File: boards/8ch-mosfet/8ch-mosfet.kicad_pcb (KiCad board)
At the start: 2 copper layers, 184.5 x 137 mm, 148 parts, among them J1 N2K, J10 Screw_Terminal_01x02, J11 Screw_Terminal_01x02, J12 Screw_Terminal_01x02, J2 I2C, J3 Screw_Terminal_01x08, J5 Screw_Terminal_01x02, J6 Screw_Terminal_01x02, J7 Screw_Terminal_01x02, J8 Screw_Terminal_01x02, J9 Screw_Terminal_01x02, M1 Fan_4pin, Q1 BC817, Q10 IRF4905, Q11 BC817, Q12 IRF4905, Q13 BC817, Q14 IRF4905, Q15 BC817, Q16 IRF4905, Q2 IRF4905, Q3 BC817, Q4 IRF4905, Q5 BC817, Q6 IRF4905, Q7 BC817, Q8 IRF4905, Q9 BC817, U1 ESP32-DEVKITC, U10 ACS725xLCTR-20AU, U11 ACS725xLCTR-20AU, U12 ACS725xLCTR-20AU, U2 MCP3208, U3 R-78B3.3-2.0, U5 ACS725xLCTR-20AU, U6 ACS725xLCTR-20AU, U7 ACS725xLCTR-20AU, U8 ACS725xLCTR-20AU, U9 ACS725xLCTR-20AU

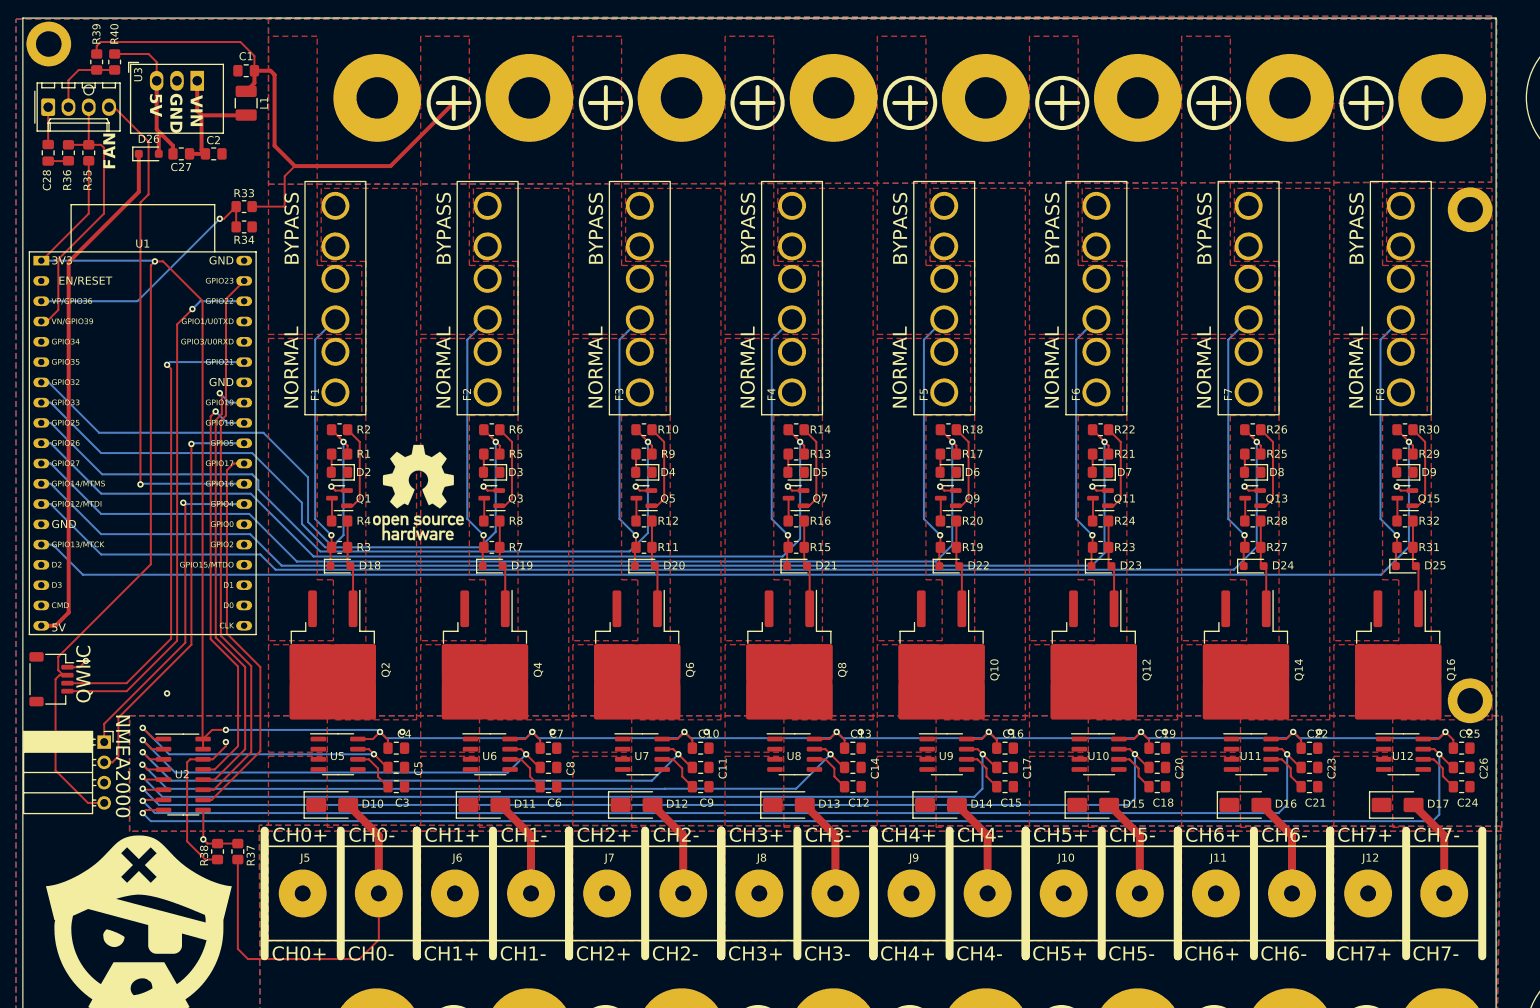
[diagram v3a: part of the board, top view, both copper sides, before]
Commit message: added 2nd fan header and simplified circuit.
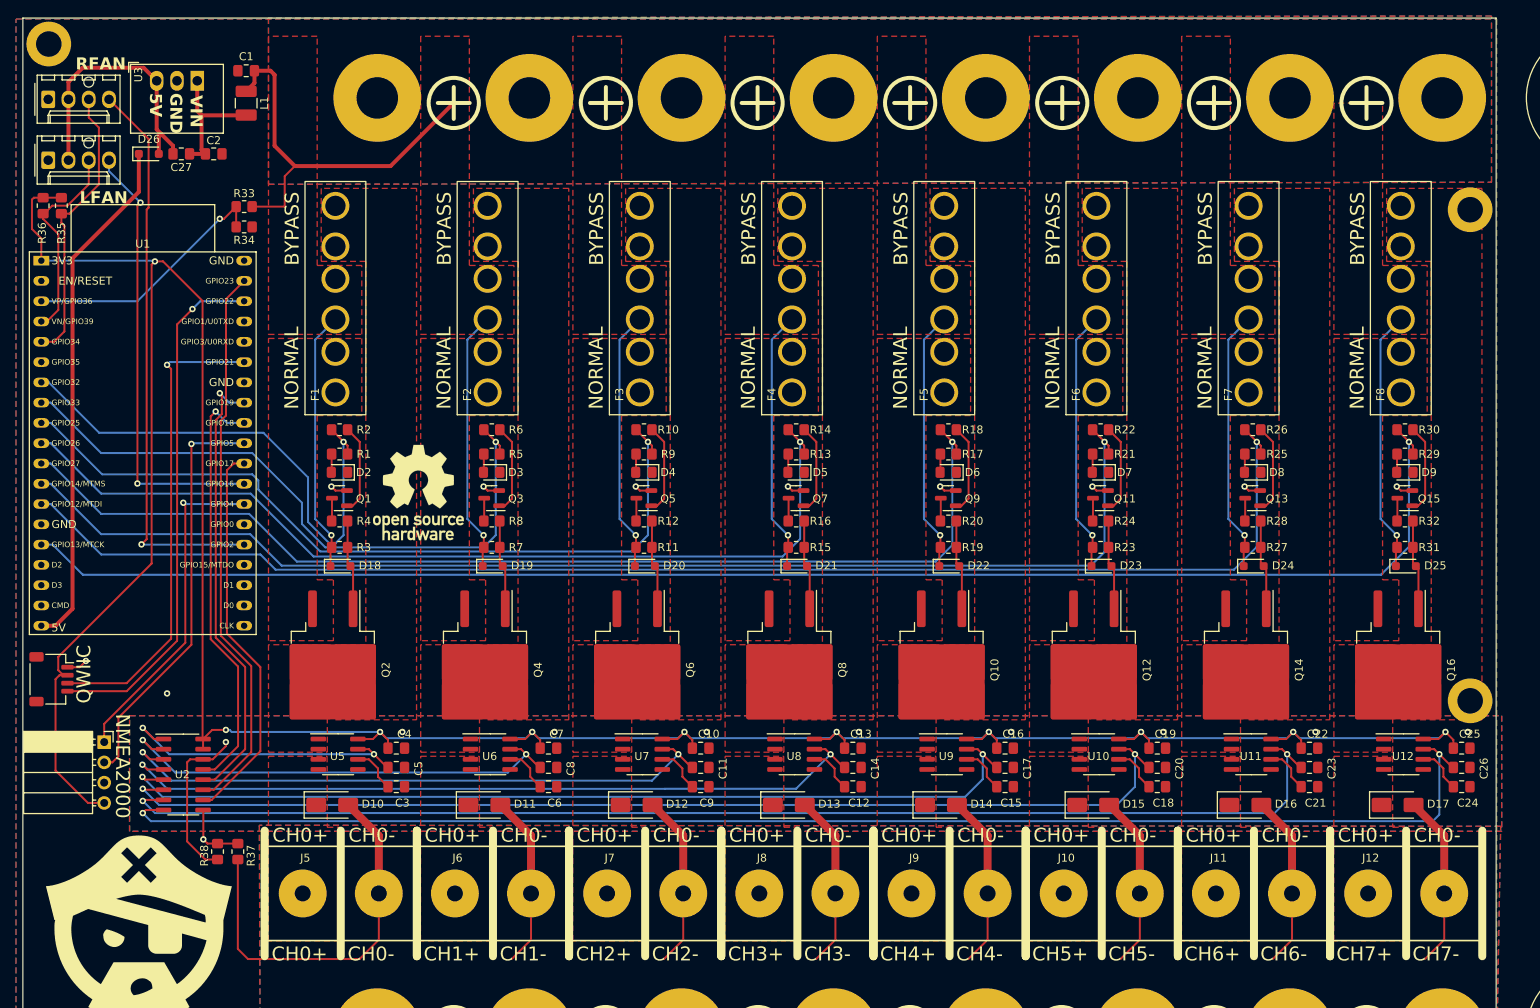
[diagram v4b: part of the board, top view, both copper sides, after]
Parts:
- removed C28: 1nF, Capacitor_SMD:C_0805_2012Metric_Pad1.18x1.45mm_HandSolder
- removed R39, R40: 0R, Resistor_SMD:R_0805_2012Metric_Pad1.20x1.40mm_HandSolder
- added M2: Fan_4pin, gnarboard:Molex 0470531000, F.Cu at (3.17, 17.8)
- R35: value 10k -> 1k
- R36: value 3.3k -> 1k
- moved R35 7.46 mm to (4.83, 23.5), turned to 90 degrees
- moved R36 7.34 mm to (2.54, 23.5)
- moved M1 0.98 mm to (3.17, 10.2)
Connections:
- M1 pad 2: Net-(M1-+) -> +5V
- M1 pad 3: FAN_TACHO -> FAN_TACH2
- M1 pad 4: FAN_PWM -> FAN_PWM2
- R35 pad 1: FAN_TACHO -> FAN_TACH2
- R36 pad 1: Net-(C28-Pad1) -> FAN_TACH1
- R36 pad 2: FAN_TACHO -> +3.3V
- U1 pad 24: unconnected-(U1-GPIO2-Pad24) -> FAN_PWM2
- U1 pad 27: FAN_PWM -> FAN_PWM1
- U1 pad 4: FAN_TACHO -> FAN_TACH1
- U1 pad 5: unconnected-(U1-GPIO34-Pad5) -> FAN_TACH2
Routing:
- net FAN_PWM2: track 0.00 -> 71.0 mm, vias 0 -> 1
- net GNDPWR: track 137.5 -> 202.1 mm
- net FAN_PWM: track 63.1 -> 0.00 mm, vias 1 -> 0
- net FAN_PWM1: track 0.00 -> 55.7 mm, vias 0 -> 2
- net FAN_TACH2: track 0.00 -> 35.7 mm
- net FAN_TACHO: track 34.7 -> 0.00 mm
- net FAN_TACH1: track 0.00 -> 25.8 mm
- net +24V: track 339.5 -> 316.0 mm
- net +5V: track 20.7 -> 34.9 mm
- net Net-(M1-+): track 9.69 -> 0.00 mm
- net GNDD: track 32.9 -> 28.3 mm
- net +3.3V: track 377.3 -> 374.3 mm
- net Net-(C28-Pad1): track 2.56 -> 0.00 mm
- net /ADC5: track 138.3 -> 137.5 mm
- net /ADC4: track 118.5 -> 117.8 mm
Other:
- board text added: "LFAN"
- board text added: "RFAN"
- board text removed: "FAN"

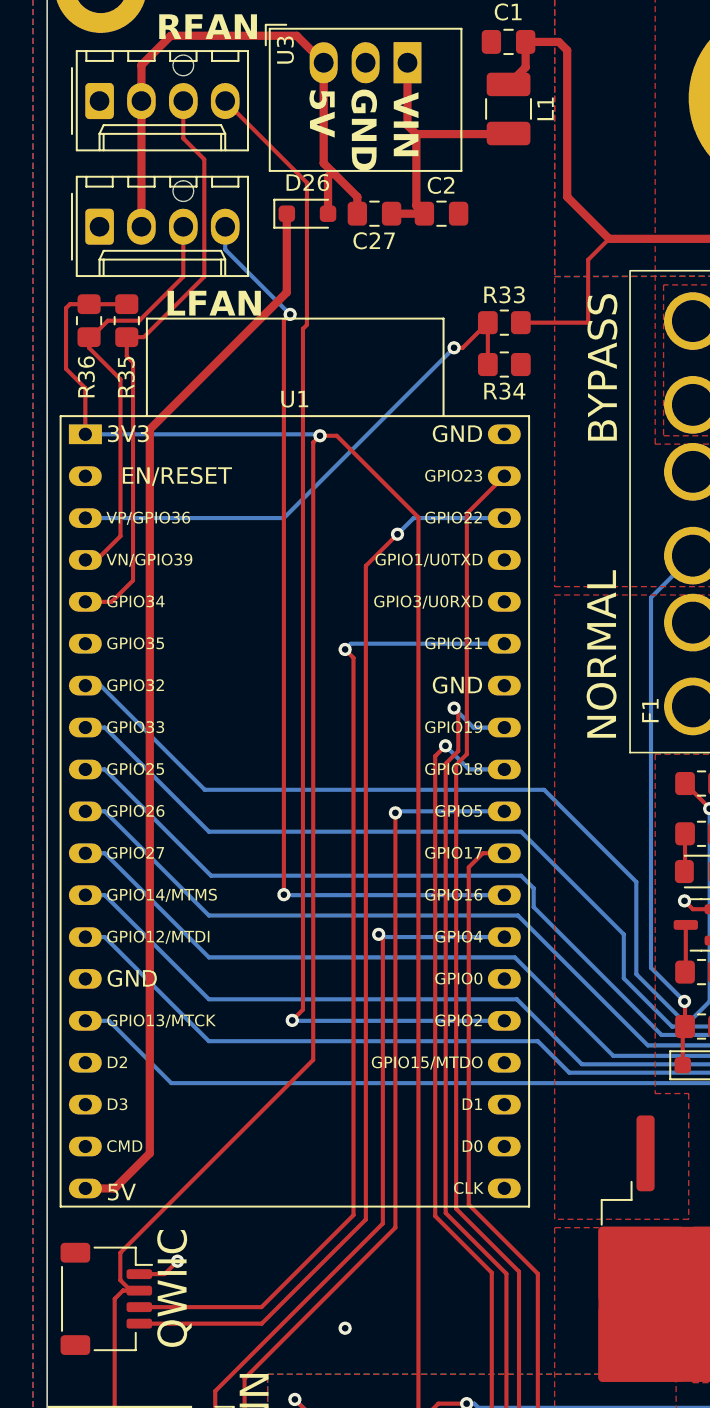
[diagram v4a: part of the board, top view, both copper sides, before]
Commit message: added a better adc for getting bus voltage
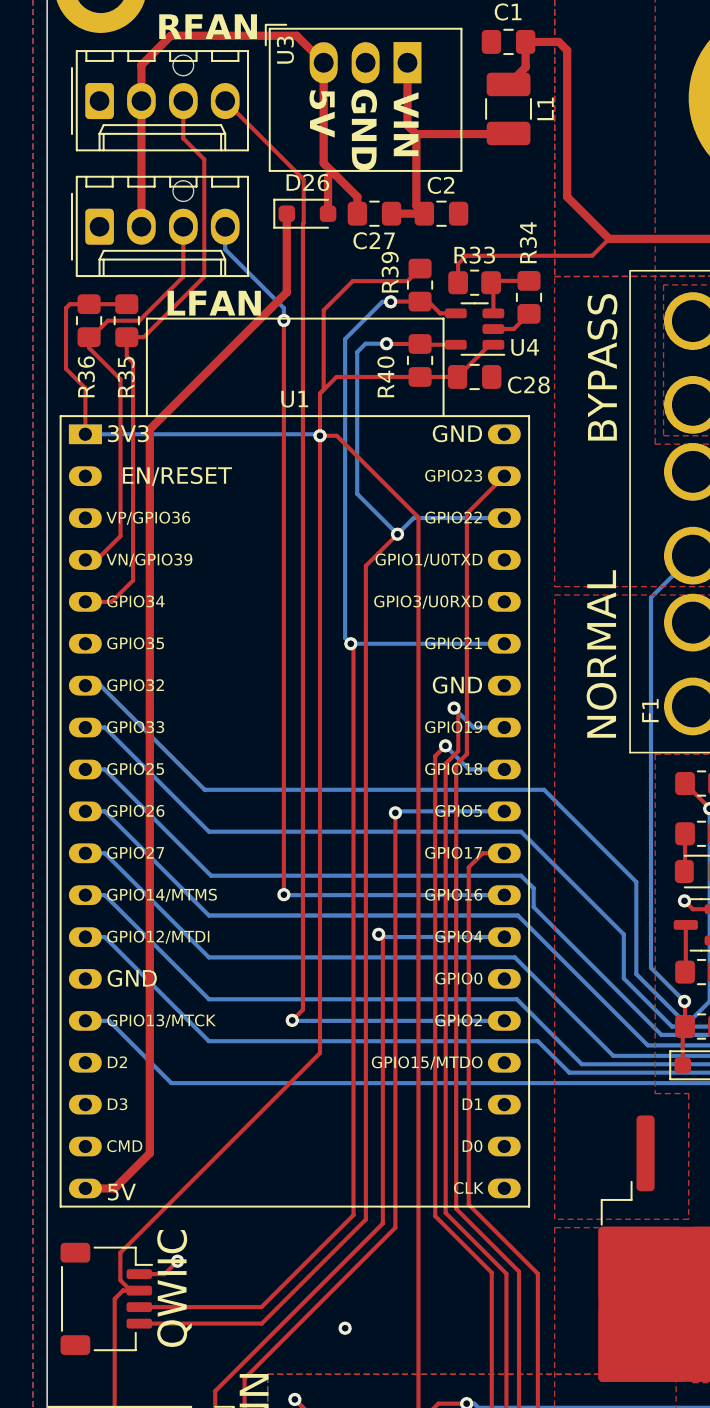
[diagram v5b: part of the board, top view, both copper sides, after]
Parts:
- added C28: 1nF, Capacitor_SMD:C_0805_2012Metric_Pad1.18x1.45mm_HandSolder, F.Cu at (25.9, 26.9)
- added R39: 2.2K, Resistor_SMD:R_0805_2012Metric_Pad1.20x1.40mm_HandSolder, F.Cu at (22.6, 21.3)
- added R40: 2.2K, Resistor_SMD:R_0805_2012Metric_Pad1.20x1.40mm_HandSolder, F.Cu at (22.6, 25.9)
- added U4: ~, Package_TO_SOT_SMD:SOT-23-5, F.Cu at (25.9, 24.0)
- R33: value 100k -> 130K
- R34: value 10k -> 16K
- moved R34 4.34 mm to (29.2, 22.1), turned to 90 degrees
- moved R33 3.02 mm to (25.9, 21.2), turned to 180 degrees
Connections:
- R33 pad 1: Net-(U1-GPIO36) -> Net-(U4-AIN)
- R34 pad 2: Net-(U1-GPIO36) -> Net-(U4-AIN)
- U1 pad 3: Net-(U1-GPIO36) -> unconnected-(U1-GPIO36-Pad3)
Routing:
- net Net-(U1-GPIO36): track 31.8 -> 0.00 mm, vias 1 -> 0
- net +3.3V: track 374.3 -> 400.8 mm
- net SDA: track 59.6 -> 85.9 mm, vias 1 -> 2
- net SCL: track 65.6 -> 83.8 mm, vias 1 -> 2
- net Net-(U4-AIN): track 0.00 -> 4.26 mm
- net GNDD: track 28.3 -> 30.8 mm
- net +24V: track 316.0 -> 317.2 mm

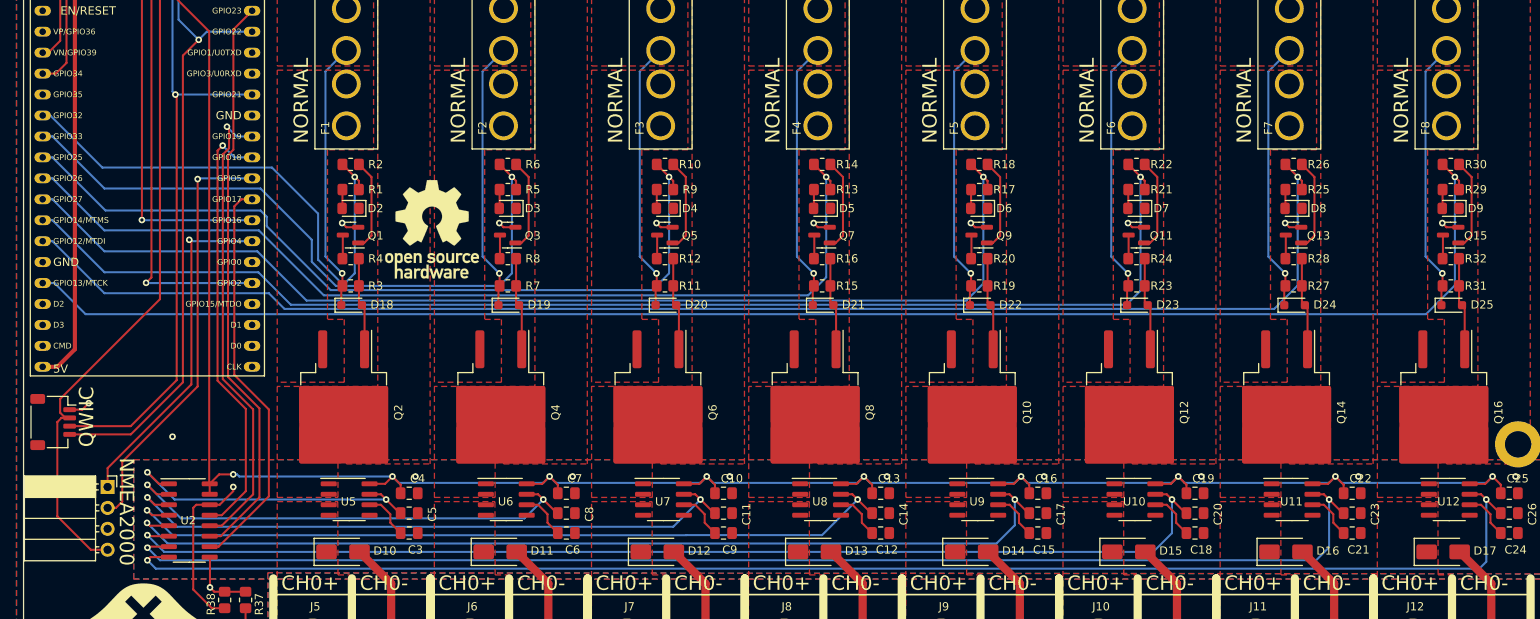
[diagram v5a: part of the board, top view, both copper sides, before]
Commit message: a couple tweaks to mosfet circuit
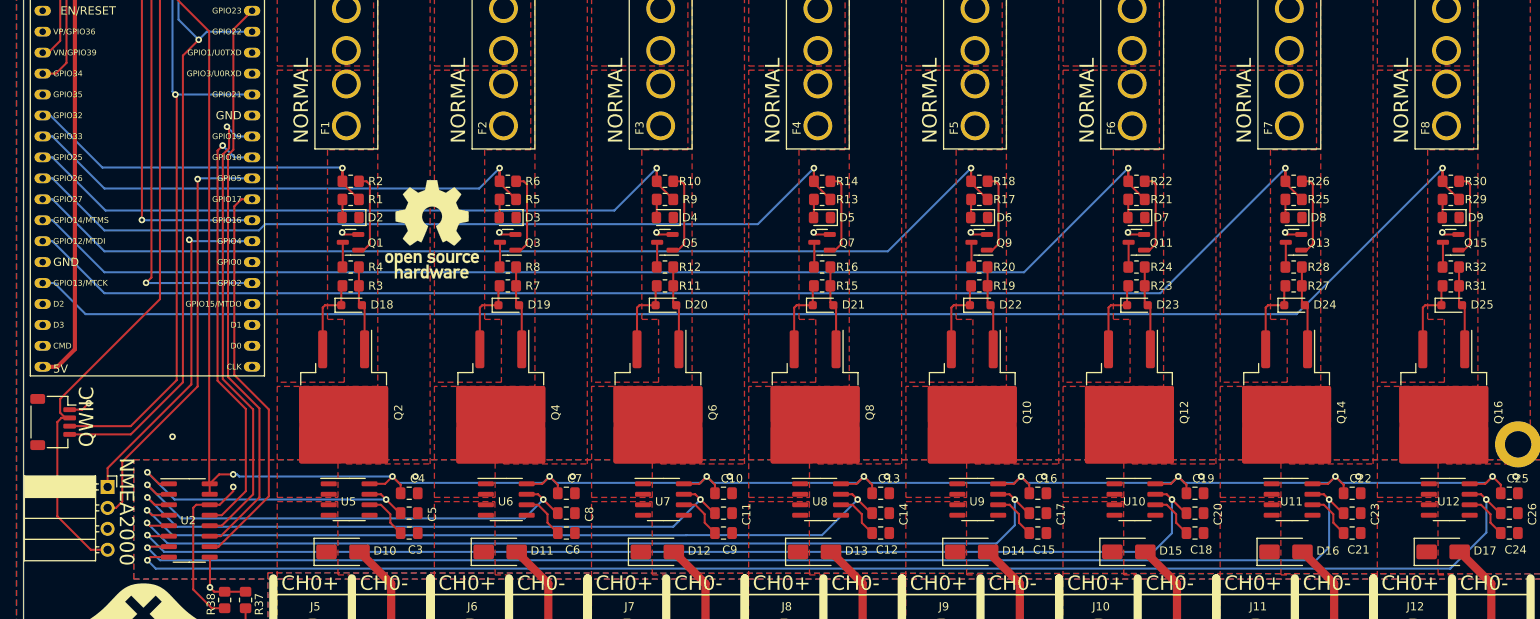
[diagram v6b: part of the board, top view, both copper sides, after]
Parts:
- Q1, Q11, Q13, Q15, Q3, Q5, Q7, Q9: value BC817 -> 2N7002
- R10, R14, R18, R2, R22, R26, R30, R6: value 10k -> 220
- U4: value ~ -> MCP3221A0T
- moved R10 2.05 mm to (77.8, 53.6)
- moved R14 2.05 mm to (96.8, 53.6)
- moved R18 2.05 mm to (115.9, 53.6)
- moved R2 2.05 mm to (39.7, 53.6)
- moved R22 2.05 mm to (135.0, 53.6)
- moved R26 2.05 mm to (154.0, 53.6)
- moved R30 2.05 mm to (173.1, 53.6)
- moved R6 2.05 mm to (58.7, 53.6)
- moved R1 1.20 mm to (39.7, 55.8)
- moved R13 1.20 mm to (96.8, 55.8)
- moved R17 1.20 mm to (115.9, 55.8)
- moved R21 1.20 mm to (135.0, 55.8)
- moved R25 1.20 mm to (154.0, 55.8)
- moved R29 1.20 mm to (173.1, 55.8)
- moved R5 1.20 mm to (58.7, 55.8)
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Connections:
- D18 pad 1: +24V -> Net-(D18-K)
- D19 pad 1: +24V -> Net-(D19-K)
- D20 pad 1: +24V -> Net-(D20-K)
- D21 pad 1: +24V -> Net-(D21-K)
- D22 pad 1: +24V -> Net-(D22-K)
- D23 pad 1: +24V -> Net-(D23-K)
- D24 pad 1: +24V -> Net-(D24-K)
- D25 pad 1: +24V -> Net-(D25-K)
- F1 pad 1: Net-(Q2-S) -> Net-(D18-K)
- F2 pad 1: Net-(Q4-S) -> Net-(D19-K)
- F3 pad 1: Net-(Q6-S) -> Net-(D20-K)
- F4 pad 1: Net-(Q8-S) -> Net-(D21-K)
- F5 pad 1: Net-(Q10-S) -> Net-(D22-K)
- F6 pad 1: Net-(Q12-S) -> Net-(D23-K)
- F7 pad 1: Net-(Q14-S) -> Net-(D24-K)
- F8 pad 1: Net-(Q16-S) -> Net-(D25-K)
- Q10 pad 3: Net-(Q10-S) -> Net-(D22-K)
- Q12 pad 3: Net-(Q12-S) -> Net-(D23-K)
- Q14 pad 3: Net-(Q14-S) -> Net-(D24-K)
- Q16 pad 3: Net-(Q16-S) -> Net-(D25-K)
- Q2 pad 3: Net-(Q2-S) -> Net-(D18-K)
- Q4 pad 3: Net-(Q4-S) -> Net-(D19-K)
- Q6 pad 3: Net-(Q6-S) -> Net-(D20-K)
- Q8 pad 3: Net-(Q8-S) -> Net-(D21-K)
- R11 pad 2: +24V -> Net-(D20-K)
- R15 pad 2: +24V -> Net-(D21-K)
- R19 pad 2: +24V -> Net-(D22-K)
- R23 pad 2: +24V -> Net-(D23-K)
- R27 pad 2: +24V -> Net-(D24-K)
- R3 pad 2: +24V -> Net-(D18-K)
- R31 pad 2: +24V -> Net-(D25-K)
- R7 pad 2: +24V -> Net-(D19-K)
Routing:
- net +24V: track 317.2 -> 52.3 mm, vias 8 -> 0
- net /PWM0: track 65.5 -> 45.2 mm
- net /PWM1: track 82.2 -> 65.3 mm
- net /PWM2: track 99.7 -> 85.5 mm
- net /PWM3: track 117.9 -> 105.5 mm
- net /PWM4: track 136.8 -> 125.6 mm
- net Net-(D19-K): track 0.00 -> 10.1 mm
- net Net-(D25-K): track 0.00 -> 10.1 mm
- net Net-(D24-K): track 0.00 -> 10.1 mm
- net Net-(D23-K): track 0.00 -> 10.1 mm
- net Net-(D22-K): track 0.00 -> 10.1 mm
- net Net-(D21-K): track 0.00 -> 10.1 mm
- net Net-(D20-K): track 0.00 -> 10.1 mm
- net Net-(D18-K): track 0.00 -> 10.1 mm
- net /PWM5: track 155.8 -> 145.7 mm
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- added copper zone on F.Cu, net Net-(D18-K)
- added copper zone on F.Cu, net Net-(D19-K)
- added copper zone on F.Cu, net Net-(D20-K)
- added copper zone on F.Cu, net Net-(D21-K)
- added copper zone on F.Cu, net Net-(D22-K)
- added copper zone on F.Cu, net Net-(D23-K)
- added copper zone on F.Cu, net Net-(D24-K)
- added copper zone on F.Cu, net Net-(D25-K)
- removed copper zone on F.Cu, net Net-(Q10-S)
- removed copper zone on F.Cu, net Net-(Q12-S)
- removed copper zone on F.Cu, net Net-(Q14-S)
- removed copper zone on F.Cu, net Net-(Q16-S)
- removed copper zone on F.Cu, net Net-(Q2-S)
- removed copper zone on F.Cu, net Net-(Q4-S)
- removed copper zone on F.Cu, net Net-(Q6-S)
- removed copper zone on F.Cu, net Net-(Q8-S)
